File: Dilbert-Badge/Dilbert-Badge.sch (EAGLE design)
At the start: 22 parts, among them IC1 MCP23017SO, J1 I2C, J2 UART, J6 IO_B, J7 IO_A, SW1 UP, SW2 DOWN, SW3 LEFT, SW4 RIGHT, SW5 A, SW6 B, SW7 RESET, SW8 SWD

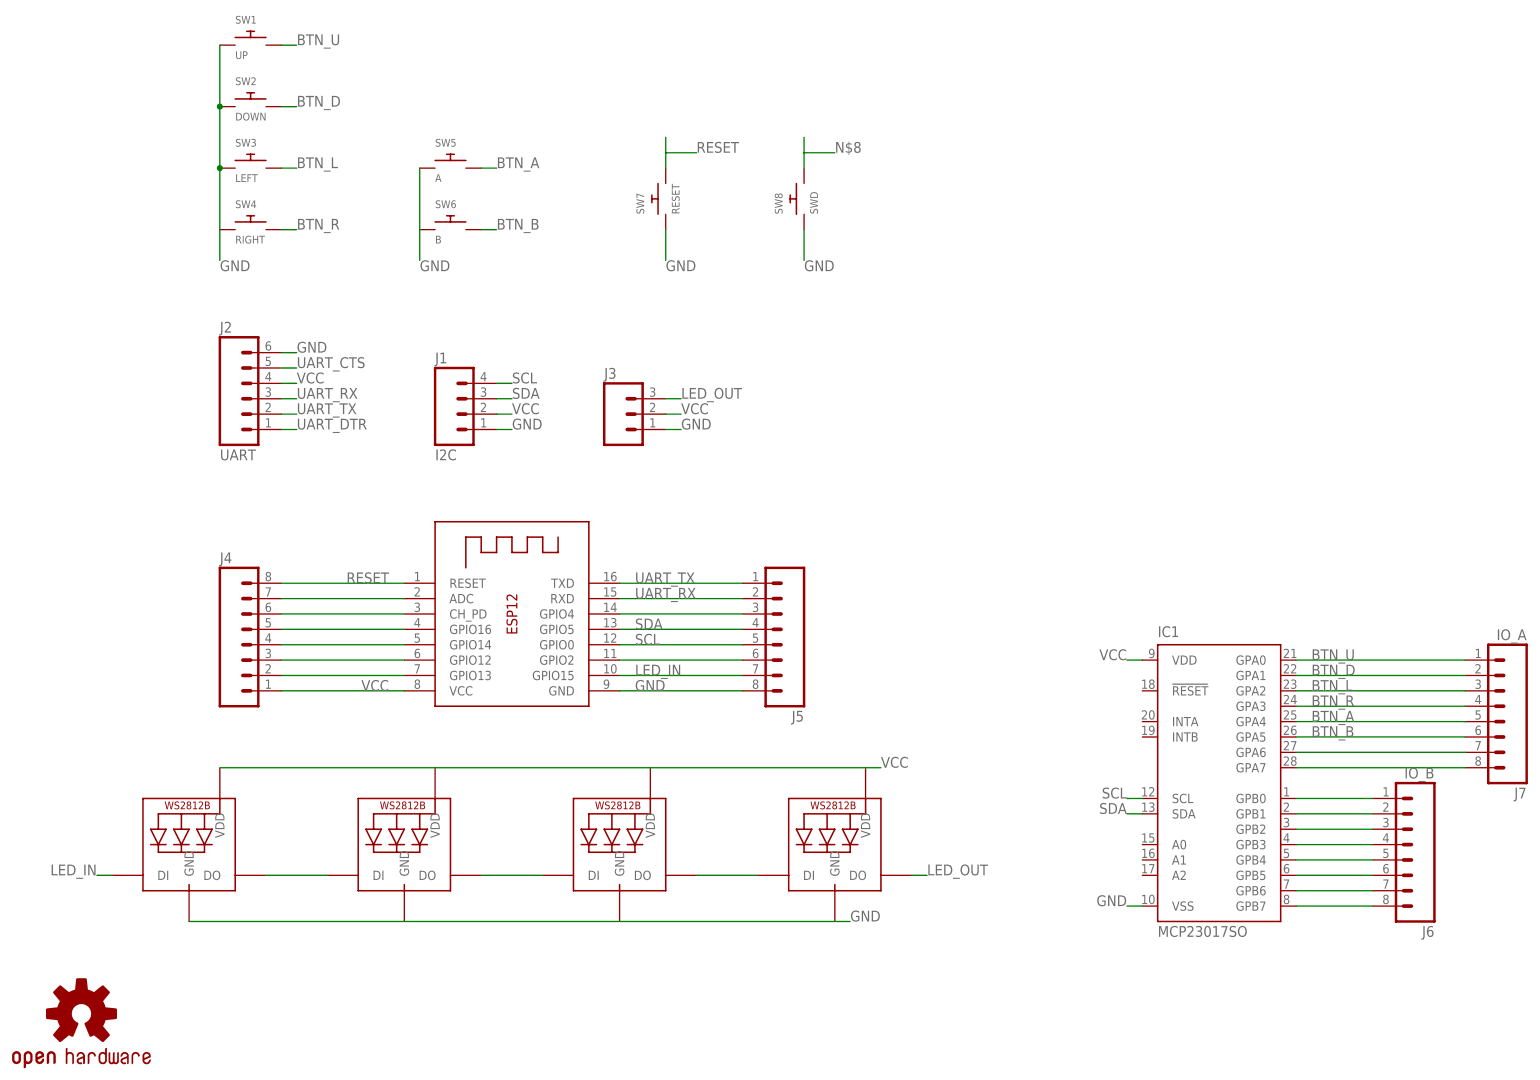
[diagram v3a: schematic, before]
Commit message: add puller resistors and decouping
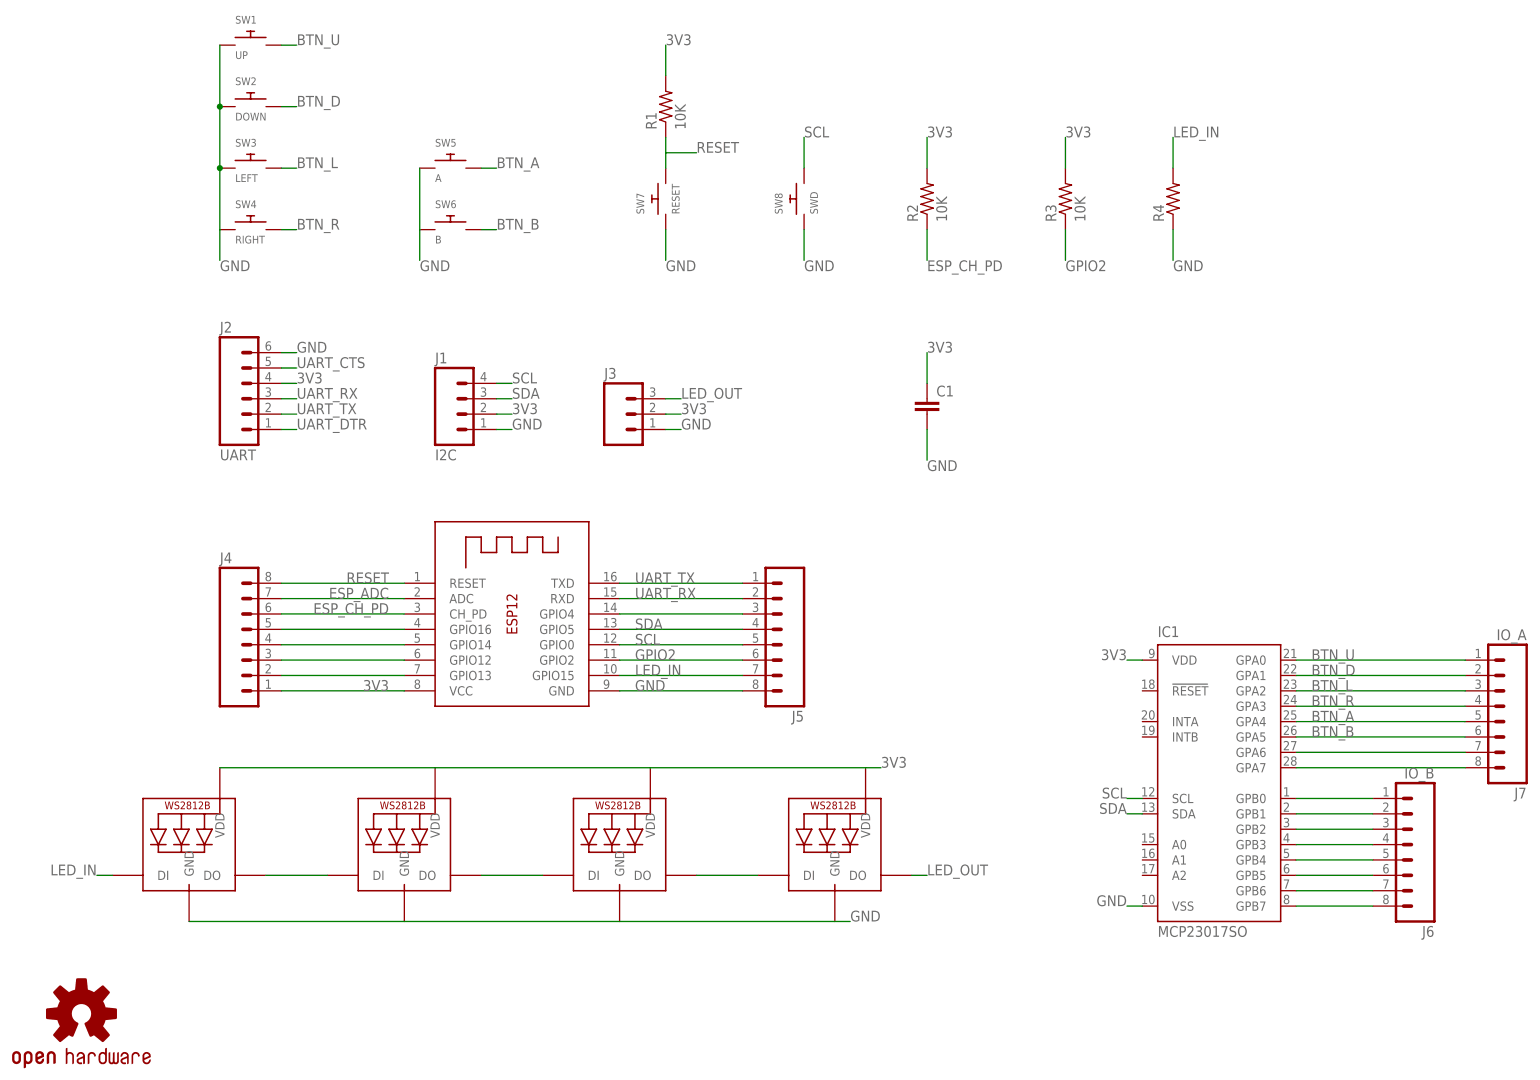
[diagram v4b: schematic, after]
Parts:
- added C1: (no value), SparkFun-Capacitors:10UF10V10%(0805)
- added R1, R2, R3: 10K, adafruit:R-US_R0805
- added R4: (no value), adafruit:R-US_R0805
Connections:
- net N$4 renamed ESP_ADC
- removed net N$13: J5.6, X1.GPIO2
- removed net N$6: J4.6, X1.CH_PD
- removed net N$8: SW8.P$2
- removed net VCC: IC1.VDD, J1.2, J2.4, J3.2, J4.1, LED1.VDD, LED2.VDD, LED3.VDD, LED4.VDD, X1.VCC
- new net 3V3: C1.1, IC1.VDD, J1.2, J2.4, J3.2, J4.1, LED1.VDD, LED2.VDD, LED3.VDD, LED4.VDD, R1.2, R2.2, R3.2, X1.VCC
- new net ESP_CH_PD: J4.6, R2.1, X1.CH_PD
- new net GPIO2: J5.6, R3.1, X1.GPIO2
- net GND: now also C1.2, R4.1
- net LED_IN: now also R4.2
- net RESET: now also R1.1
- net SCL: now also SW8.P$2
